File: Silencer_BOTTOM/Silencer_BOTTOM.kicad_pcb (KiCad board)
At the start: 2 copper layers, 80 x 175 mm, 45 parts, among them IC1 TL072, IC2 AS3360, IC3 TL072, IC4 AS3360, J1 Conn_02x05_Odd_Even

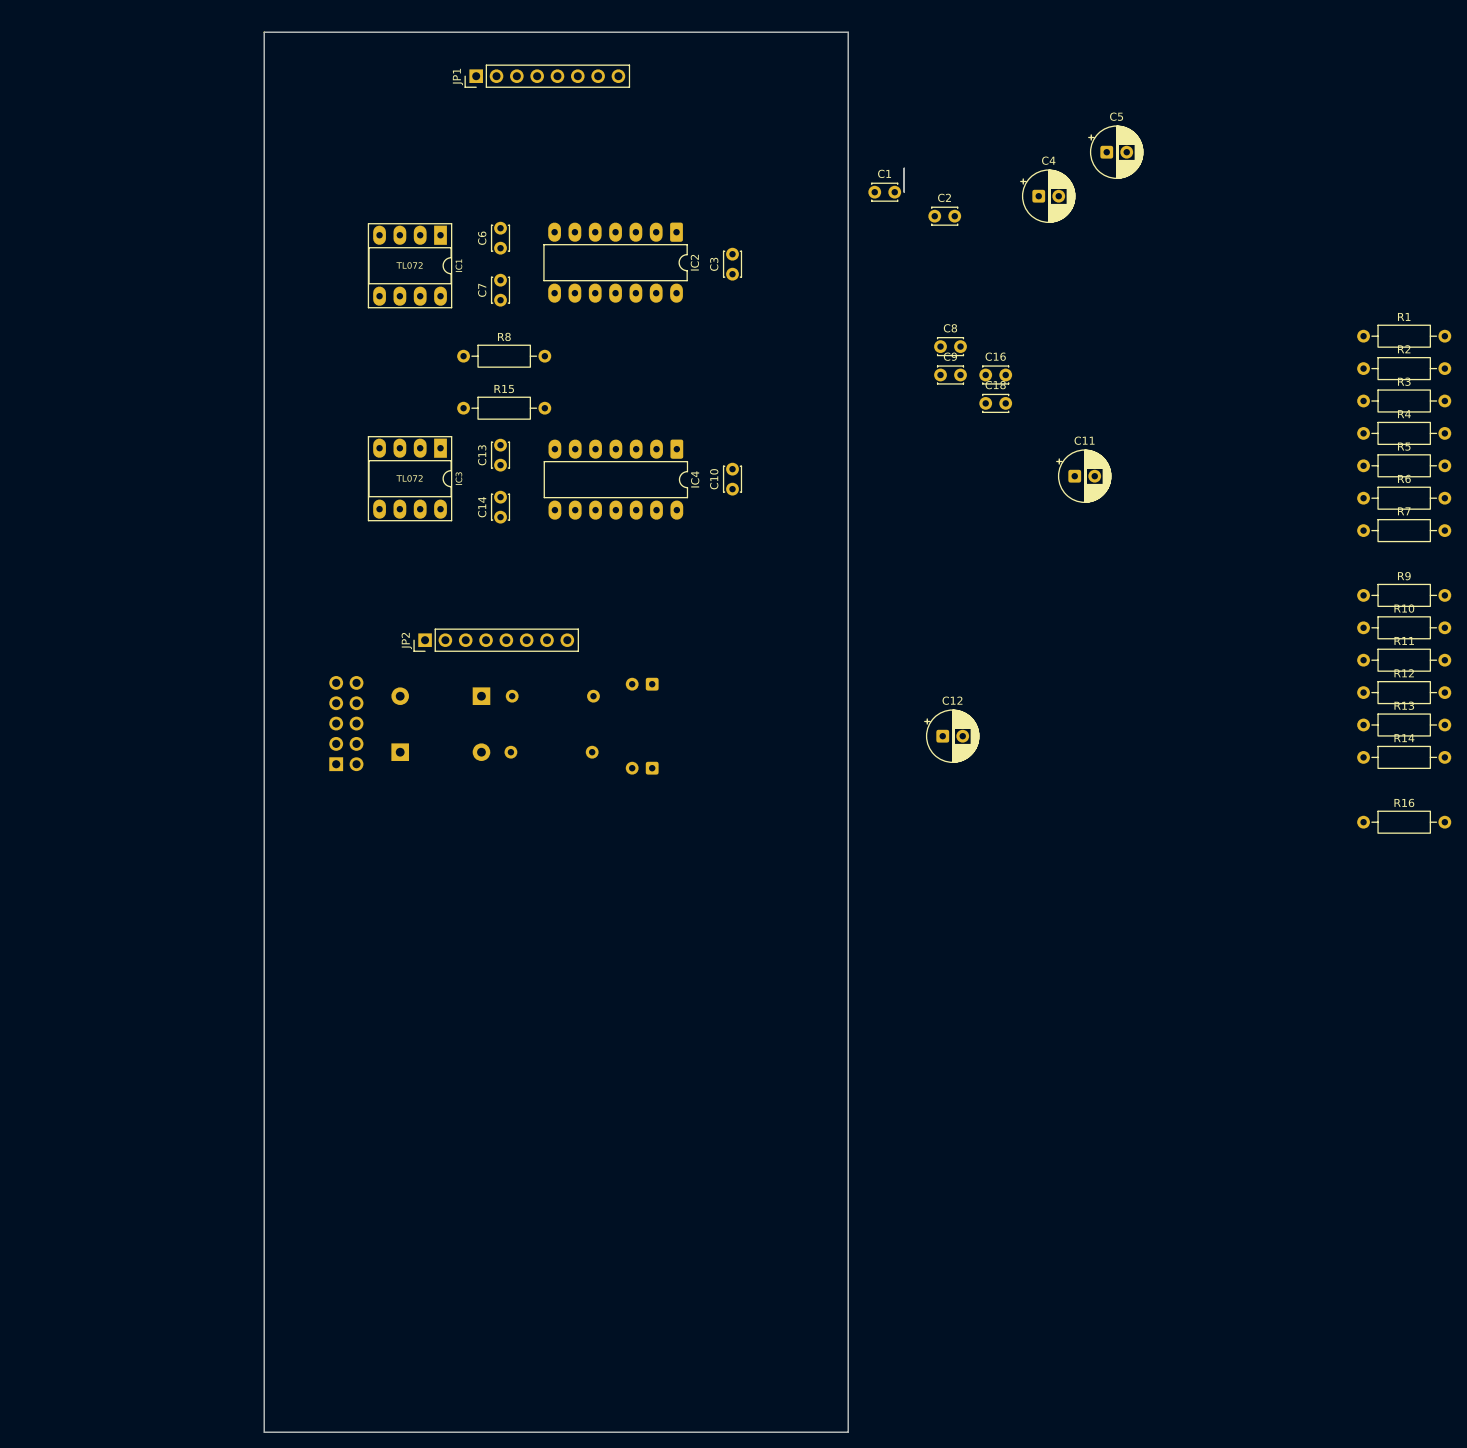
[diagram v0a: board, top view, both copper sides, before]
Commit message: Bottom board layout roughed out.  Routing began
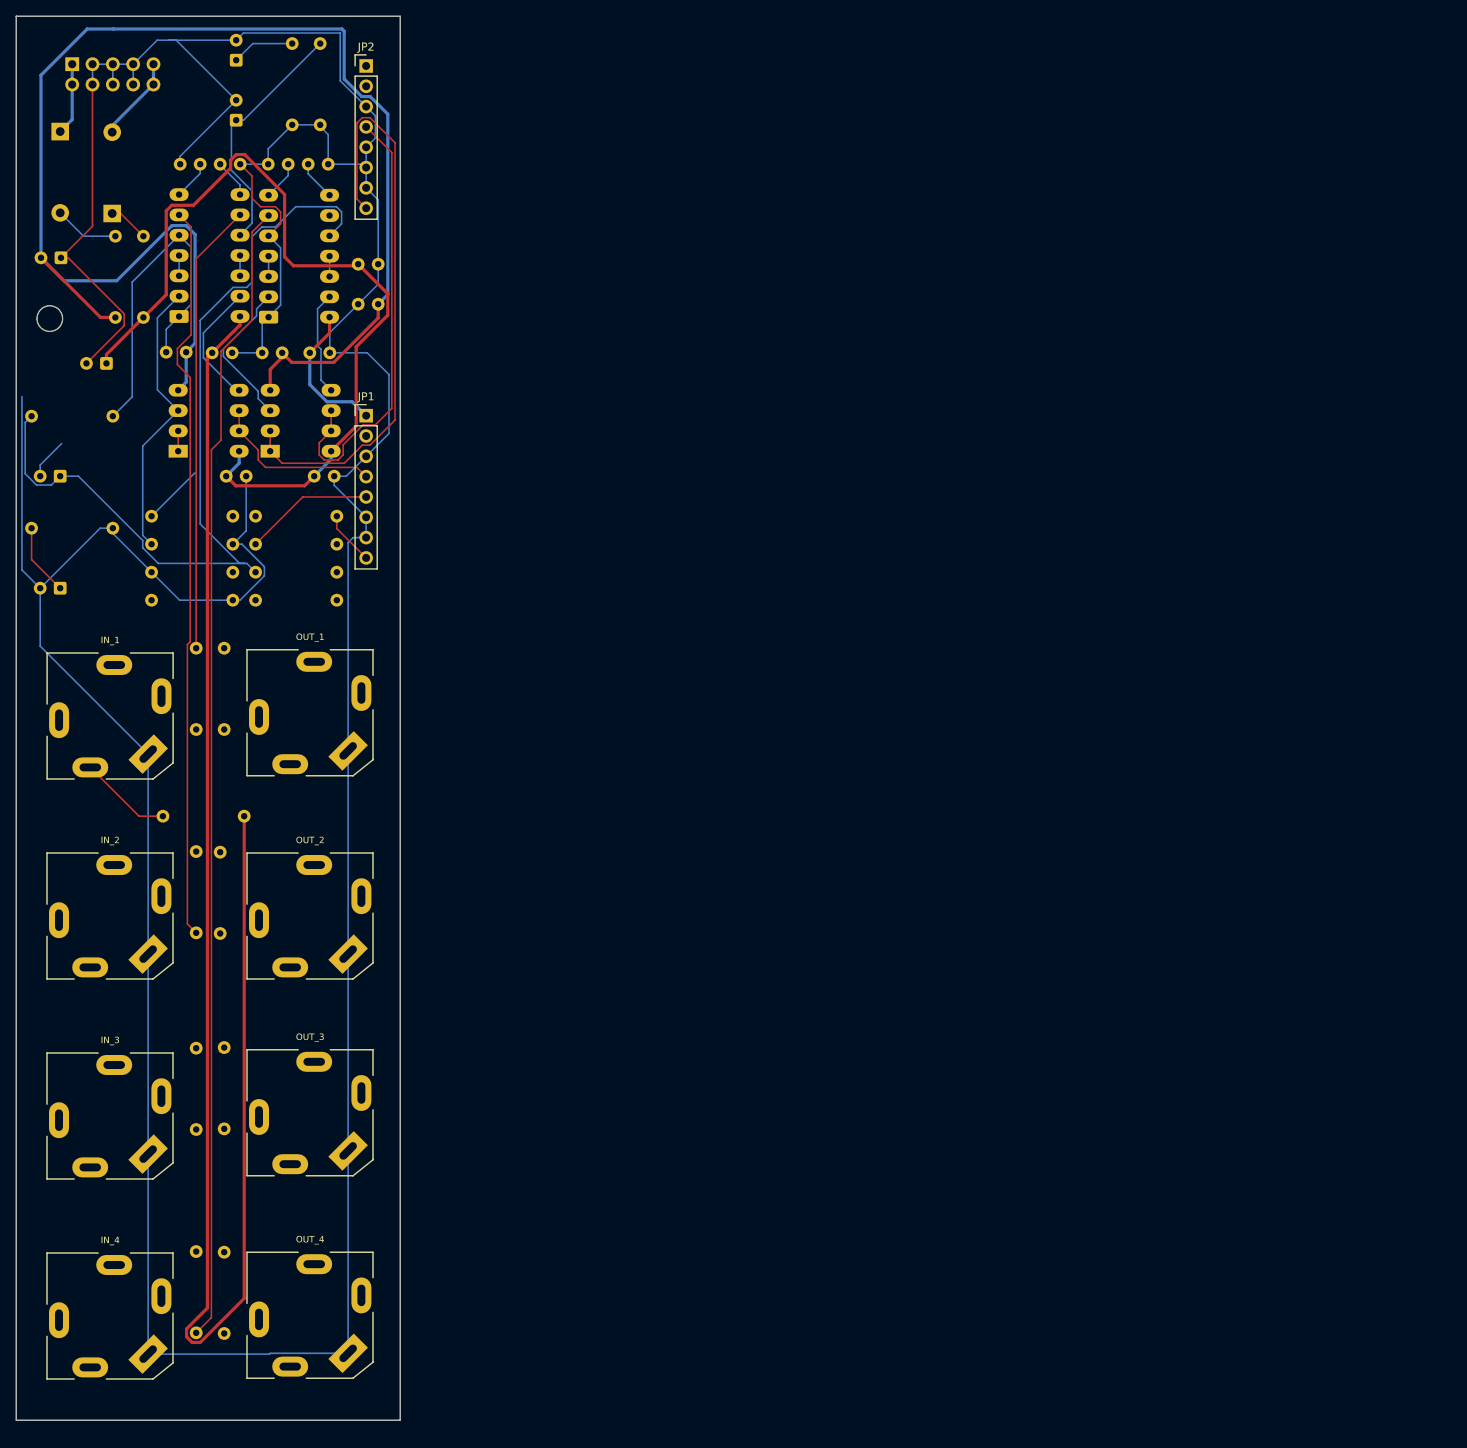
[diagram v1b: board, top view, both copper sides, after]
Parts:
- added IN_1: AudioJack2_SwitchT, AO_tht:Jack_6.35mm_PJ_629HAN_slots, F.Cu at (12.8, 100.0)
- added IN_2: AudioJack2_SwitchT, AO_tht:Jack_6.35mm_PJ_629HAN_slots, F.Cu at (12.8, 125.0)
- added IN_3: AudioJack2_SwitchT, AO_tht:Jack_6.35mm_PJ_629HAN_slots, F.Cu at (12.8, 150.0)
- added IN_4: AudioJack2_SwitchT, AO_tht:Jack_6.35mm_PJ_629HAN_slots, F.Cu at (12.8, 175.0)
- added OUT_1: AudioJack2_SwitchT, AO_tht:Jack_6.35mm_PJ_629HAN_slots, F.Cu at (37.8, 99.6)
- added OUT_2: AudioJack2_SwitchT, AO_tht:Jack_6.35mm_PJ_629HAN_slots, F.Cu at (37.8, 125.0)
- added OUT_3: AudioJack2_SwitchT, AO_tht:Jack_6.35mm_PJ_629HAN_slots, F.Cu at (37.8, 149.6)
- added OUT_4: AudioJack2_SwitchT, AO_tht:Jack_6.35mm_PJ_629HAN_slots, F.Cu at (37.8, 174.9)
- added R101: 1K, AO_tht:R_Axial_DIN0207_L6.3mm_D2.5mm_P10.16mm_Horizontal, B.Cu at (27.0, 91.5)
- added R104: 1K, AO_tht:R_Axial_DIN0207_L6.3mm_D2.5mm_P10.16mm_Horizontal, B.Cu at (26.5, 117.0)
- added R106: 1K, AO_tht:R_Axial_DIN0207_L6.3mm_D2.5mm_P10.16mm_Horizontal, B.Cu at (27.0, 141.4)
- added R111: 4K7, AO_tht:R_Axial_DIN0207_L6.3mm_D2.5mm_P10.16mm_Horizontal, B.Cu at (29.5, 112.5)
- added R112: 1K, AO_tht:R_Axial_DIN0207_L6.3mm_D2.5mm_P10.16mm_Horizontal, B.Cu at (27.0, 167.0)
- added REF**: MountingHole_3.2mm_M3, AO_tht:MountingHole_3.2mm_M3, F.Cu at (5.20, 50.3)
- C1, C10, C11, C12, C13, C14, C16, C18, C2, C3, C4, C5, C6, C7, C8, C9, IC1, IC2, IC3, IC4, R1, R10, R11, R12, R13, R14, R15, R16, R2, R3, R4, R5, R6, R7, R8, R9: moved to B.Cu
- moved R12 170.0 mm to (2.92, 62.5)
- moved R11 167.3 mm to (2.92, 76.5)
- moved R1 153.7 mm to (17.9, 78.5)
- moved R2 152.6 mm to (17.9, 75.0)
- moved R10 151.5 mm to (17.9, 85.5)
- moved R9 151.5 mm to (17.9, 82.0)
- moved R16 148.6 mm to (23.5, 141.5), turned to -90 degrees
- moved R7 146.7 mm to (23.5, 91.5), turned to -90 degrees
- moved R3 141.2 mm to (35.5, 15.9), turned to -90 degrees
- moved R5 140.7 mm to (39.0, 15.9), turned to -90 degrees
- moved R14 140.4 mm to (30.9, 82.0)
- moved R13 139.4 mm to (30.9, 85.5)
- moved R4 138.9 mm to (30.9, 75.0)
- moved R6 138.6 mm to (30.9, 78.5)
- moved C11 127.6 mm to (6.50, 84.0), turned to 180 degrees
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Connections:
- JP2 pad 3: IN4_B -> GND_1
- JP2 pad 5: IN3_B -> GND_1
- JP2 pad 6: IN1_B -> GND_1
- JP2 pad 7: IN2_B -> GND_1
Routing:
- net GND_1: track 0.00 -> 603.2 mm
- net +12V_1: track 0.00 -> 218.5 mm
- net -12V: track 0.00 -> 179.1 mm
- net Net-(IC4-II1): track 0.00 -> 143.4 mm
- net +12V: track 0.00 -> 107.7 mm
- net Net-(IC4-VC2): track 0.00 -> 106.6 mm
- net Net-(IC2-II1): track 0.00 -> 92.3 mm
- net LED4_B: track 0.00 -> 73.1 mm
- net Net-(IC2-II2): track 0.00 -> 56.4 mm
- net LED3_B: track 0.00 -> 55.4 mm
- net Net-(IC1A-+): track 0.00 -> 35.5 mm
- net Net-(IC2-VC2): track 0.00 -> 30.9 mm
- net LED1_B: track 0.00 -> 21.5 mm
- net Net-(IC3A-+): track 0.00 -> 19.0 mm
- net M2_B: track 0.00 -> 16.3 mm
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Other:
- board size 80 x 175 mm -> 48 x 175.5 mm

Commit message: Routed and silkscreen cleaned up
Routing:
- net Net-(IC4-II2): track 0.00 -> 130.0 mm, vias 0 -> 1
- net -12V: track 179.1 -> 63.0 mm
- net +12V_1: track 218.5 -> 106.0 mm
- net LED3_B: track 55.4 -> 141.2 mm, vias 0 -> 1
- net M4_B: track 0.00 -> 83.6 mm, vias 0 -> 2
- net LED2_B: track 2.54 -> 83.5 mm, vias 0 -> 1
- net LED4_B: track 73.1 -> 146.1 mm, vias 0 -> 3
- net M3_B: track 0.00 -> 67.6 mm
- net Net-(C5-Pad1): track 7.86 -> 73.0 mm
- net IN2_B: track 0.00 -> 56.8 mm
- net IN3_B: track 0.00 -> 54.5 mm
- net IN1_B: track 0.00 -> 54.5 mm
- net Net-(IC3B-+): track 13.0 -> 50.2 mm, vias 0 -> 2
- net LED1_B: track 21.5 -> 58.3 mm, vias 0 -> 1
- net Net-(IC2-VC2): track 30.9 -> 67.7 mm
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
